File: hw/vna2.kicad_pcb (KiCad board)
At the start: 4 copper layers, 73.9 x 85.7 mm, 522 parts, among them CON1 BARREL_JACK, P1 SMA, P10 CONN_01X01, P11 CONN_01X01, P12 CONN_01X01, P13 CONN_01X01, P14 CONN_01X01, P15 CONN_01X01, P16 CONN_01X01, P17 MNT, P18 MNT, P19 MNT, P2 SMA, P20 CLIP, P21 CLIP, P22 CLIP, P23 CLIP, P24 CLIP, P25 CLIP, P26 TP, P27 TP, P28 CONN_01X01, P3 CONN_01X01, P4 SMA, P5 CONN_01X01, P6 SMA, P7 SMA, P8 SMA, P9 CONN_01X01, SW1 SW_PUSH, SW2 SW_PUSH, T1 TCM1-63AX+, U1 KT2520K-40MHz, U10 PE42420, U11 PE42420, U12 TRF37A75, U13 SKY13322-375LF, U14 5515LP15A730, U15 LP0603A0902ANTR, U16 3550LP14A300, U17 LP0603A1880ANTR, U18 SKY13322-375LF, U19 L7980, U2 NB3N551, U20 L7980, U21 ADA4932-1, U22 TSV911, U23 MIC5366-1.8YC5, U24 HMC713LP3E, U25 MCP1824T-3302E, U26 TRF37A75, U27 PE42420, U28 PE42420, U29 PE42420, U3 PE43711, U30 XC7A15T-1FTG256C, U31 USB-MICRO, U32 93LC46B, U33 FT2232D, U34 LTC2247, U35 TSV911, U36 LP5907-3V3, U37 L7980, U38 L7980, U39 LP5907-3V0, U4 LP5907-3V3, U40 W25Q32JV, U41 LP5907(DNP), U42 NC7S04P5X, U5 MAX2871, U6 PE42420, U7 ADL5801, U8 LP5907-3V3, U9 MAX2871, Y1 ABMM-6.000MHZ

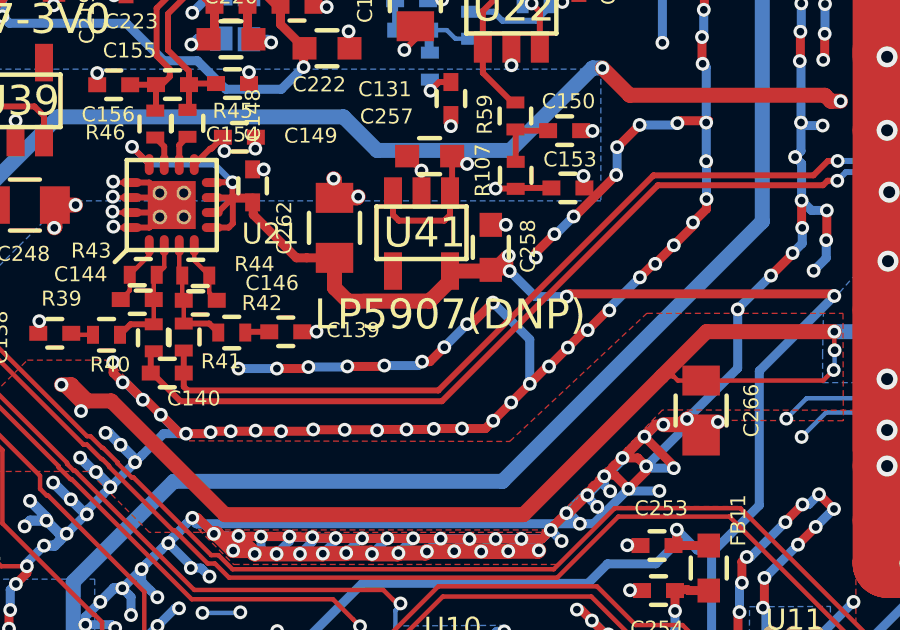
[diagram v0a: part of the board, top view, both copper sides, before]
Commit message: Update components values
Change IF amplifier to ADA4940. Same footprint, no changes in PCB.
Fix M[0:2] connections.
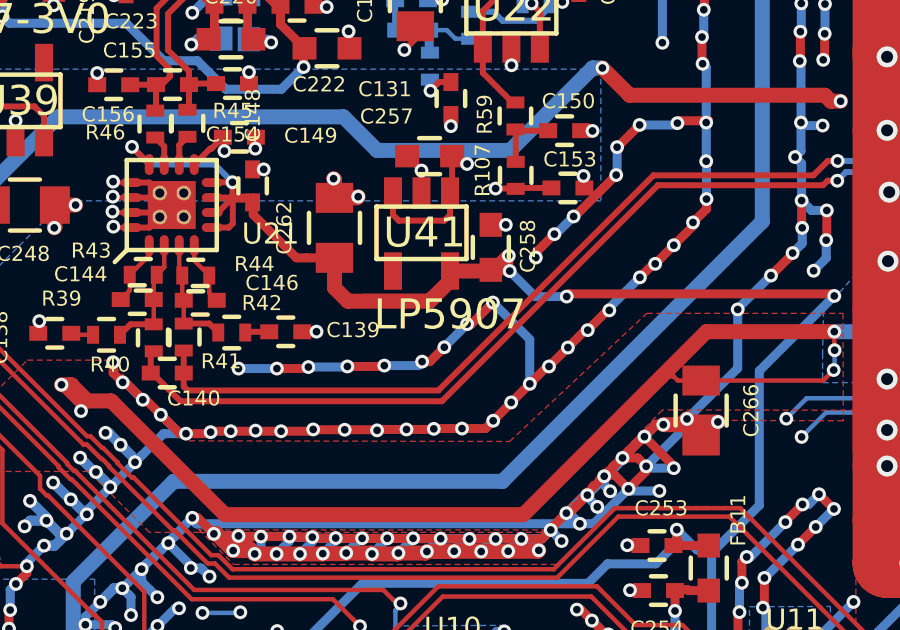
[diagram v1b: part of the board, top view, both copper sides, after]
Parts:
- C109: value 10n -> 4.7n
- C257, C258: value DNP -> 1u
- L6, L7: value CIC21P101NE -> 0
- R110: value 1k -> DNP
- R115, R121: value 0 -> DNP
- R116: value DNP -> 0
- R50, R51: value 100 -> 1k
- R58: value 6.8k -> 8.2k
- R65: value 56 -> 100
- SW1: value SW_PUSH -> DNP
- U21: value ADA4932-1 -> ADA4940-1
- U41: value LP5907(DNP) -> LP5907
